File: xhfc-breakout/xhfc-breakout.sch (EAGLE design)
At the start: 93 parts, among them Q1 BC848CSMD, Q2 BC848CSMD, Q3 BC848CSMD, Q4 BC848CSMD, U1 XHFC-2SU, X1 UEXT

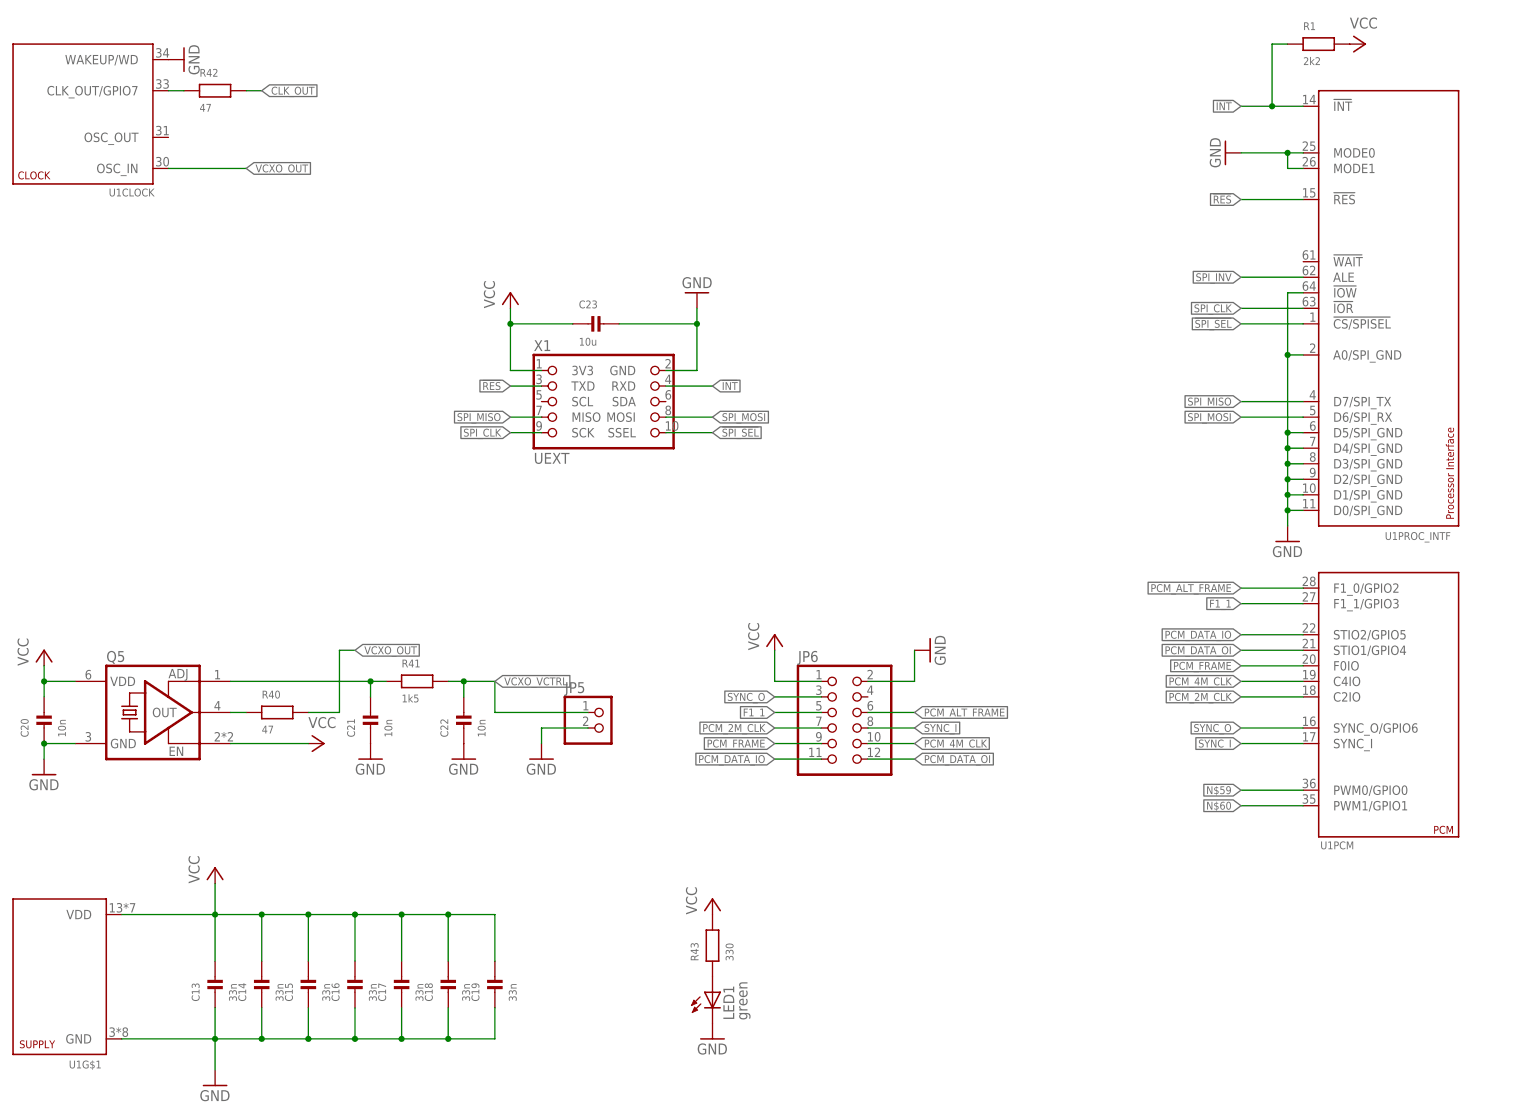
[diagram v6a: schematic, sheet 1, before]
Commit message: xhfc-breakout: Fix some part values; documentation
* R18 + R34 are 330k and not 3k9
* R5, R6, R21, R22 are 3R3 instead of 62R in universal TE/NT
* add various documentation text snippets
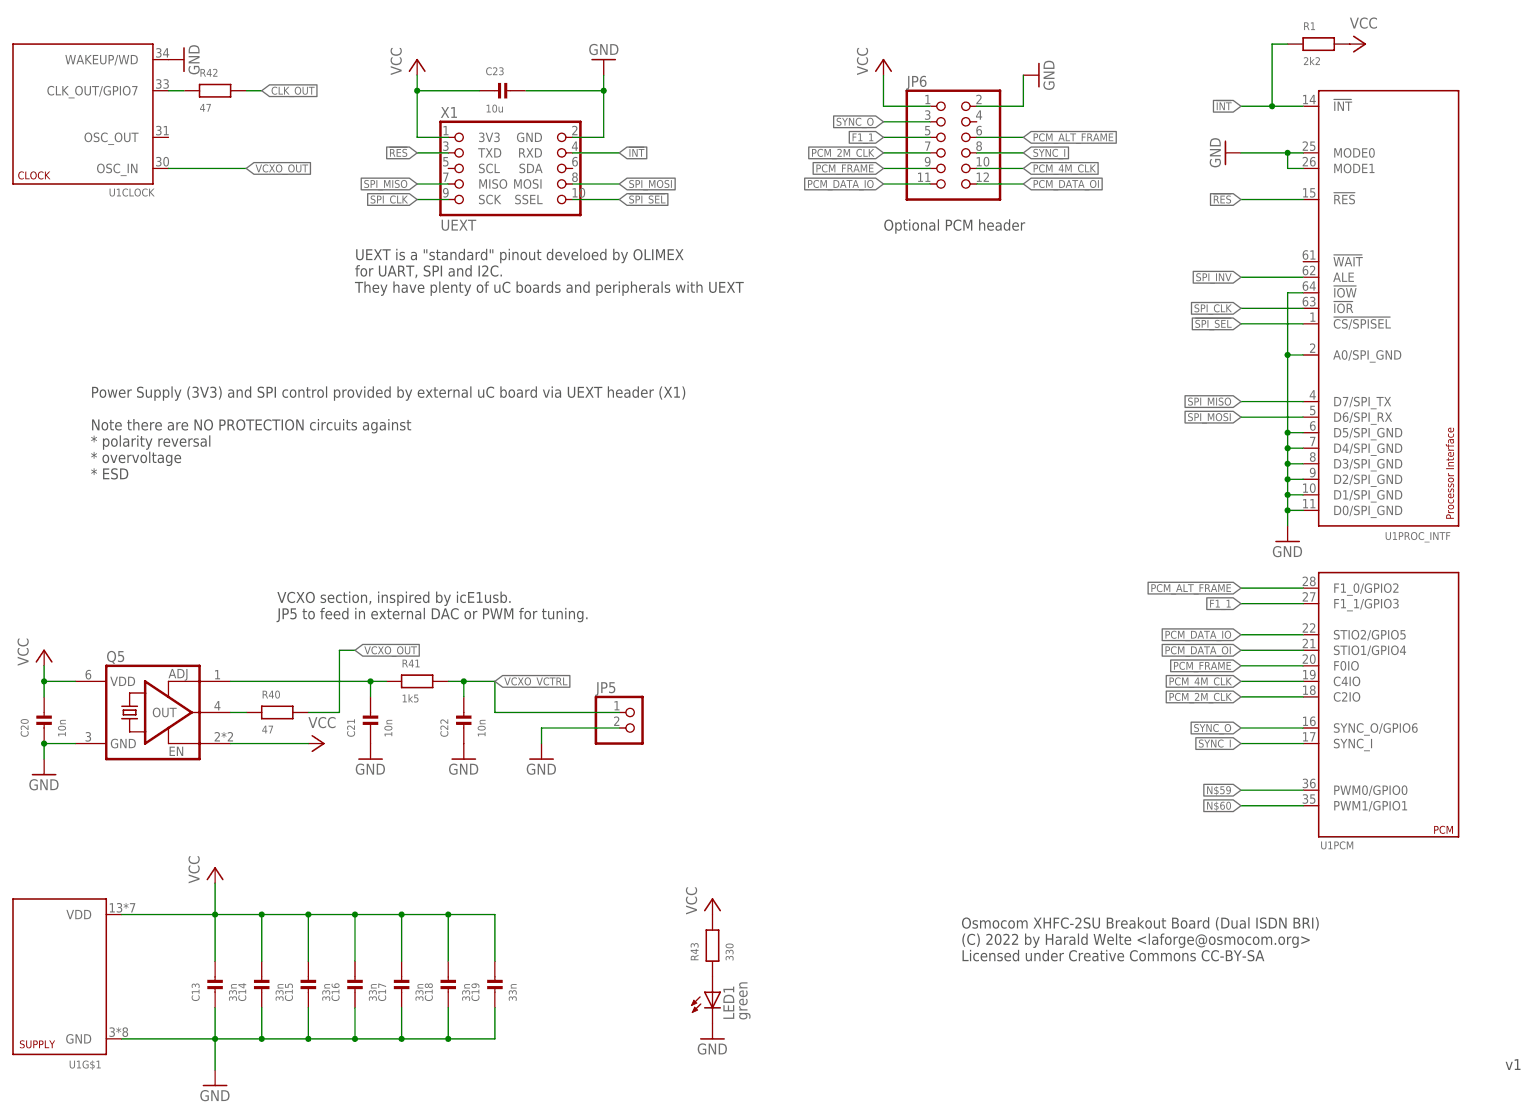
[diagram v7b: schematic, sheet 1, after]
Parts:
- R18, R34: value 3k9 -> 330k
- R21: value 62 -> 62 (3R3 universaal)
- R22, R5, R6: value 62 -> 62 (3R3 universal)
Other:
- note added: "JP1/JP2 can be used for phantom power supply of the S0 bus."
- note added: "JP3/JP4 are for TE/NT cross-over. Put the jumpers either * vertical |||| or * horizontal =="
- note added: "Optional PCM header"
- note added: "Osmocom XHFC-2SU Breakout Board (Dual ISDN BRI) (C) 2022 by Harald Welte <laforge@osmocom.org> Licensed under Creative Commons CC-BY-SA"
- note added: "Power Supply (3V3) and SPI control provided by external uC board via UEXT header (X1) Note there are NO PROTECTION circuits against * polarity reversal * overvoltage * ESD"
- note added: "R19, R20, R35, R36 are S0 bus termination. You may not always want them. Later board should probably have DIP switch"
- note added: "UEXT is a "standard" pinout develoed by OLIMEX for UART, SPI and I2C. They have plenty of uC boards and peripherals with UEXT"
- note added: "VCXO section, inspired by icE1usb. JP5 to feed in external DAC or PWM for tuning."
- note added: "VDD_SU biasing: * populate only either D1/D10 or the dashed section * D1/D10 is for NT-only mode * dashed box is for universal TE/NT mode * R5, R6, R21, R22 are 3.3Ohms in universal/TE mode"
- moved on the sheet: C23, JP5, JP6, X1

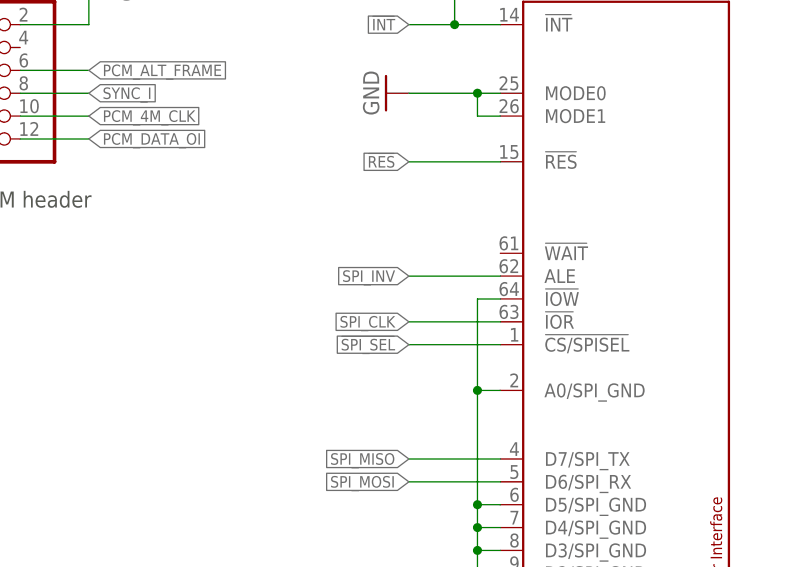
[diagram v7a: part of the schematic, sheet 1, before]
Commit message: xhfc-breaout: Conncet SPI_INV to GND
This was missing from the v1 design. SPI_INV must be tied to either high
or low to select the SPI clock polarity.  It was tied to low by manawyrm
in his manual rework, so let's reflect this in the design accordingly.
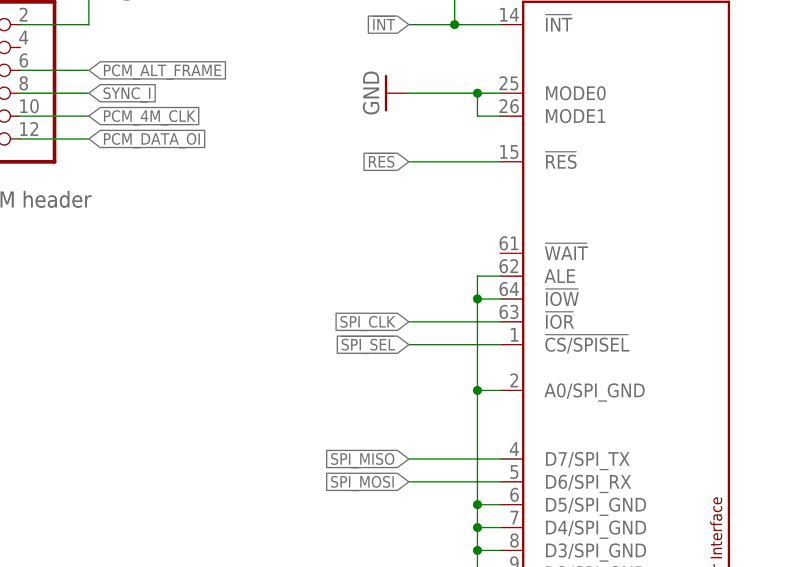
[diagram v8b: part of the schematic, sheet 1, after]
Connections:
- removed net SPI_INV: U1PROC_INTF.ALE
- net GND: now also U1PROC_INTF.ALE
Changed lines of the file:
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@@
 <wire x1="218.44" y1="134.62" x2="218.44" y2="124.46" width="0.1524" layer="91"/>
 <junction x="218.44" y="124.46"/>
+<pinref part="U1" gate="PROC_INTF" pin="ALE"/>
+<wire x1="220.98" y1="137.16" x2="218.44" y2="137.16" width="0.1524" layer="91"/>
+<wire x1="218.44" y1="137.16" x2="218.44" y2="134.62" width="0.1524" layer="91"/>
+<junction x="218.44" y="134.62"/>
 </segment>
 <segment>
@@
 </segment>
 </net>
-<net name="SPI_INV" class="0">
-<segment>
-<pinref part="U1" gate="PROC_INTF" pin="ALE"/>
-<wire x1="220.98" y1="137.16" x2="210.82" y2="137.16" width="0.1524" layer="91"/>
-<label x="210.82" y="137.16" size="1.27" layer="95" rot="R180" xref="yes"/>
-</segment>
-</net>
